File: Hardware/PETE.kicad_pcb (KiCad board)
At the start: 4 copper layers, 16 parts, among them U3 LM66200DRLR, U4 MAX77827AEFD+T, U5 SC4215

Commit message: PCB Done
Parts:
- added 3V3: 3V3LED, Resistor_SMD:R_0402_1005Metric, F.Cu at (66.4, 39.7)
- added 3V3: TestPoint, TestPoint:TestPoint_Pad_D1.0mm, F.Cu at (54.7, 25.9)
- added 3V3: TestPoint, TestPoint:TestPoint_Pad_D1.0mm, F.Cu at (64.2, 31.0)
- added BBIN: TestPoint, TestPoint:TestPoint_Pad_D1.0mm, F.Cu at (62.6, 29.1)
- added BBIN: TestPoint, TestPoint:TestPoint_Pad_D1.0mm, F.Cu at (49.8, 37.1)
- added BOOT: Conn_01x02_Male, Connector_PinHeader_2.54mm:PinHeader_1x02_P2.54mm_Vertical, F.Cu at (71.6, 20.6)
- added C1: 10uF, Capacitor_SMD:C_0402_1005Metric, F.Cu at (64.7, 36.4)
- added C10: 0.1uF, Capacitor_SMD:C_0402_1005Metric, F.Cu at (75.4, 33.4)
- added C11: 0.1uF, Capacitor_SMD:C_0402_1005Metric, F.Cu at (73.5, 43.2)
- added C12: 4.2pF, Capacitor_SMD:C_0402_1005Metric, F.Cu at (68.3, 33.9)
- added C13: C, Capacitor_SMD:C_0402_1005Metric, F.Cu at (74.6, 30.1)
- added C14: C, Capacitor_SMD:C_0402_1005Metric, F.Cu at (70.7, 30.1)
- added C15: 100nF, Capacitor_SMD:C_0402_1005Metric, F.Cu at (62.4, 41.9)
- added C16: 10uF, Capacitor_SMD:C_0402_1005Metric, F.Cu at (63.3, 41.9)
- added C17: 47nF, Capacitor_SMD:C_0402_1005Metric, F.Cu at (51.0, 43.7)
- added C18: 0.1n, Capacitor_SMD:C_0402_1005Metric, F.Cu at (91.9, 41.1)
- added C19: 0.1n, Capacitor_SMD:C_0402_1005Metric, F.Cu at (92.1, 50.0)
- added C2: 1uF, Capacitor_SMD:C_0402_1005Metric, F.Cu at (68.0, 35.8)
- added C28: 0.1n, Capacitor_SMD:C_0402_1005Metric, F.Cu at (83.2, 50.8)
- added C29: 0.1n, Capacitor_SMD:C_0402_1005Metric, F.Cu at (94.4, 35.7)
- added C3: 0.1uF, Capacitor_SMD:C_0402_1005Metric, F.Cu at (63.5, 22.9)
- added C30: 0.1n, Capacitor_SMD:C_0402_1005Metric, F.Cu at (95.2, 27.7)
- added C31: 0.1n, Capacitor_SMD:C_0402_1005Metric, F.Cu at (98.4, 41.9)
- added C32: 0.1n, Capacitor_SMD:C_0402_1005Metric, F.Cu at (98.6, 50.7)
- added C33: 0.1n, Capacitor_SMD:C_0402_1005Metric, F.Cu at (89.4, 50.9)
- added C34: 0.1n, Capacitor_SMD:C_0402_1005Metric, F.Cu at (95.3, 21.3)
- added C35: 0.1n, Capacitor_SMD:C_0402_1005Metric, F.Cu at (95.4, 29.3)
- added C36: 100nF, Capacitor_SMD:C_0402_1005Metric, F.Cu at (70.2, 45.7)
- added C37: 100nF, Capacitor_SMD:C_0402_1005Metric, F.Cu at (68.3, 44.0)
- added C4: 1uF, Capacitor_SMD:C_0402_1005Metric, F.Cu at (64.7, 34.5)
- added C5: 0.1uF, Capacitor_SMD:C_0402_1005Metric, F.Cu at (65.7, 36.4)
- added C6: 0.1uF, Capacitor_SMD:C_0402_1005Metric, F.Cu at (66.7, 36.4)
- added C7: 1uF, Capacitor_SMD:C_0402_1005Metric, F.Cu at (70.2, 33.0)
- added C8: 0.1uF, Capacitor_SMD:C_0402_1005Metric, F.Cu at (70.3, 22.9)
- added C9: 10nF, Capacitor_SMD:C_0402_1005Metric, F.Cu at (70.2, 34.0)
- added D1: SM712_SOT23, Package_TO_SOT_SMD:SOT-23, F.Cu at (49.2, 41.0)
- added D2: SP0503BAHT, Package_TO_SOT_SMD:SOT-143, F.Cu at (75.3, 45.3)
- added Data+: TestPoint, TestPoint:TestPoint_Pad_D1.0mm, F.Cu at (69.5, 53.1)
- added Data-: TestPoint, TestPoint:TestPoint_Pad_D1.0mm, F.Cu at (69.4, 50.1)
- added EN: Conn_01x02_Male, Connector_PinHeader_2.54mm:PinHeader_1x02_P2.54mm_Vertical, F.Cu at (65.4, 20.6)
- added H1: MountingHole_Pad, MountingHole:MountingHole_3.2mm_M3_DIN965_Pad, F.Cu at (103.0, 53.1)
- added H2: MountingHole_Pad, MountingHole:MountingHole_3.2mm_M3_DIN965_Pad, F.Cu at (48.0, 53.1)
- added H3: MountingHole_Pad, MountingHole:MountingHole_3.2mm_M3_DIN965_Pad, F.Cu at (48.0, 22.1)
- added H4: MountingHole_Pad, MountingHole:MountingHole_3.2mm_M3_DIN965_Pad, F.Cu at (103.0, 22.1)
- added J1: RBUS, Connector_Molex:Molex_Mini-Fit_Jr_5566-06A_2x03_P4.20mm_Vertical, F.Cu at (64.8, 53.2)
- added J2: USB_C_Receptacle_USB2.0, Connector_USB:USB_C_Receptacle_Palconn_UTC16-G, F.Cu at (76.2, 51.1)
- added J3: Micro_SD_Card_Det, Connector_Card:microSD_HC_Hirose_DM3AT-SF-PEJM5, B.Cu at (86.5, 27.8)
- added JP1: TermJP, Jumper:SolderJumper-2_P1.3mm_Open_RoundedPad1.0x1.5mm, F.Cu at (52.8, 41.5)
- added L1: 2.0nH, Inductor_SMD:L_0402_1005Metric, F.Cu at (66.2, 34.9)
- added L2: 20nH, Inductor_SMD:L_0402_1005Metric, F.Cu at (72.2, 32.9)
- added MISO: TestPoint, TestPoint:TestPoint_Pad_D1.0mm, F.Cu at (82.9, 46.8)
- added MOSI: TestPoint, TestPoint:TestPoint_Pad_D1.0mm, F.Cu at (82.9, 43.0)
- added MTCK: TestPoint, TestPoint:TestPoint_Pad_D1.0mm, F.Cu at (78.2, 32.8)
- added MTDI: TestPoint, TestPoint:TestPoint_Pad_D1.0mm, F.Cu at (78.2, 28.6)
- added MTDO: TestPoint, TestPoint:TestPoint_Pad_D1.0mm, F.Cu at (78.2, 30.4)
- added MTMS: TestPoint, TestPoint:TestPoint_Pad_D1.0mm, F.Cu at (78.1, 26.7)
- added PS1: MPRLS0025PA00001A, PressureSensor:XDCR_MPRLS0025PA00001A, F.Cu at (86.4, 50.8)
- added PS2: MPRLS0025PA00001A, PressureSensor:XDCR_MPRLS0025PA00001A, F.Cu at (95.3, 50.8)
- added PS3: MPRLS0025PA00001A, PressureSensor:XDCR_MPRLS0025PA00001A, F.Cu at (95.1, 41.9)
- added PS4: MPRLS0025PA00001A, PressureSensor:XDCR_MPRLS0025PA00001A, F.Cu at (95.4, 32.5)
- added PS5: MPRLS0025PA00001A, PressureSensor:XDCR_MPRLS0025PA00001A, F.Cu at (95.3, 24.5)
- added R1: 10K, Resistor_SMD:R_0402_1005Metric, F.Cu at (66.3, 22.9)
- added R10: 60, Resistor_SMD:R_0603_1608Metric, F.Cu at (53.0, 39.5)
- added R11: 5.1k, Resistor_SMD:R_0402_1005Metric, F.Cu at (73.1, 46.0)
- added R12: 5.1k, Resistor_SMD:R_0402_1005Metric, F.Cu at (77.6, 46.5)
- added R13: 470, Resistor_SMD:R_0402_1005Metric, F.Cu at (78.6, 46.5)
- added R18: 10k, Resistor_SMD:R_0402_1005Metric, B.Cu at (78.1, 24.6)
- added R2: 470, Resistor_SMD:R_0402_1005Metric, F.Cu at (63.9, 40.2)
- added R3: 10K, Resistor_SMD:R_0402_1005Metric, F.Cu at (67.2, 38.2)
- added R4: 470, Resistor_SMD:R_0402_1005Metric, F.Cu at (65.4, 39.7)
- added R5: 47.5, Resistor_SMD:R_0402_1005Metric, F.Cu at (68.3, 33.0)
- added R6: 499, Resistor_SMD:R_0402_1005Metric, F.Cu at (74.4, 33.4)
- added R8: 0, Resistor_SMD:R_0603_1608Metric, F.Cu at (56.0, 44.7)
- added R9: 60, Resistor_SMD:R_0603_1608Metric, F.Cu at (53.0, 43.4)
- added RXD: TestPoint, TestPoint:TestPoint_Pad_D1.0mm, F.Cu at (68.7, 30.6)
- added SCLK: TestPoint, TestPoint:TestPoint_Pad_D1.0mm, F.Cu at (82.8, 44.9)
- added SS1: TestPoint, TestPoint:TestPoint_Pad_D1.0mm, F.Cu at (82.9, 38.2)
- added SS2: TestPoint, TestPoint:TestPoint_Pad_D1.0mm, F.Cu at (85.1, 38.2)
- added SS3: TestPoint, TestPoint:TestPoint_Pad_D1.0mm, F.Cu at (87.3, 38.2)
- added SS4: TestPoint, TestPoint:TestPoint_Pad_D1.0mm, F.Cu at (80.8, 38.2)
- added SS5: TestPoint, TestPoint:TestPoint_Pad_D1.0mm, F.Cu at (78.6, 38.2)
- added TX: TX_LED, Resistor_SMD:R_0402_1005Metric, F.Cu at (63.5, 38.8)
- added TXD: TestPoint, TestPoint:TestPoint_Pad_D1.0mm, F.Cu at (68.7, 28.8)
- added U1: ESP32-S3, iclr:QFN40P700X700X90-57N, F.Cu at (73.5, 38.6)
- added U11: DPS310, iclr:XDCR_DPS310, F.Cu at (70.4, 44.0)
- added U2: SN65HVD230, Package_SO:SOIC-8_3.9x4.9mm_P1.27mm, F.Cu at (58.2, 41.2)
- added USB: USB_LED, Resistor_SMD:R_0402_1005Metric, F.Cu at (77.6, 44.6)
- added VBUS: TestPoint, TestPoint:TestPoint_Pad_D1.0mm, F.Cu at (60.1, 27.9)
- added Y1: 40MHz±10ppm, Crystal:Crystal_SMD_2016-4Pin_2.0x1.6mm, F.Cu at (72.6, 30.5)
- moved R17 146.5 mm to (49.1, 27.6), turned to 180 degrees
- moved R16 143.2 mm to (51.0, 27.6), turned to 180 degrees
- moved C27 140.8 mm to (52.8, 26.7), turned to 180 degrees
- moved C26 139.9 mm to (52.8, 27.6), turned to 180 degrees
- moved U5 139.7 mm to (50.9, 31.8), turned to 90 degrees
- moved C24 138.7 mm to (49.8, 35.9), turned to 180 degrees
- moved C25 134.8 mm to (51.9, 35.9), turned to 0 degrees
- moved C23 133.8 mm to (54.4, 31.2), turned to 90 degrees
- moved L3 131.6 mm to (57.0, 28.6), turned to 180 degrees
- moved U4 128.2 mm to (57.0, 32.3), turned to 90 degrees
- moved R15 126.0 mm to (57.2, 34.6), turned to 0 degrees
- moved C21 124.9 mm to (59.5, 31.0), turned to 90 degrees
- moved C22 122.9 mm to (59.2, 33.8), turned to -90 degrees
- moved R14 122.8 mm to (61.1, 30.2), turned to -90 degrees
- moved C20 121.3 mm to (60.2, 33.8), turned to -90 degrees
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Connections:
- net +3V3 renamed +3.3V
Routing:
- net /SCLK: track 0.00 -> 71.8 mm, vias 0 -> 7
- net /MOSI: track 0.00 -> 70.1 mm, vias 0 -> 7
- net /MISO: track 0.00 -> 69.8 mm, vias 0 -> 7
- net +3.3V: track 1.61 -> 46.6 mm, vias 1 -> 15
- net /SS5: track 0.00 -> 38.9 mm, vias 0 -> 3
- net /SS2: track 0.00 -> 37.3 mm, vias 0 -> 3
- net /SS4: track 0.00 -> 34.2 mm, vias 0 -> 3
- net /SS3: track 0.00 -> 33.8 mm, vias 0 -> 3
- net /SS1: track 0.00 -> 32.2 mm, vias 0 -> 3
- net /CHIP_PU: track 0.00 -> 28.7 mm, vias 0 -> 1
- net RBUS_uC_V: track 0.00 -> 28.0 mm, vias 0 -> 1
- net /BOOT: track 0.00 -> 25.9 mm, vias 0 -> 1
- net /TXD: track 0.00 -> 24.0 mm
- net /CAN-: track 0.00 -> 22.8 mm
- net GND: track 6.73 -> 27.7 mm, vias 8 -> 74
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- added copper zone on In2.Cu, net +3.3V
- added copper zone on B.Cu, net GND
- added copper zone on In1.Cu, net GND
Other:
- board outline added: 61 x 37 mm

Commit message: Review Changes Made (except for meme)
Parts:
- C18, C19, C28, C29, C30: value 0.1n -> 0.1u
- C31, C32, C33, C34, C35: value 0.1n -> 1n
- TP15: renamed from SCLK; moved to B.Cu
- TP16: renamed from MOSI; moved to B.Cu
- TP17: renamed from MISO; moved to B.Cu
- moved TXLED1 15.3 mm to (74.5, 28.0), turned to 180 degrees
- moved R2 14.9 mm to (72.6, 28.0), turned to 0 degrees
- moved TP9 7.81 mm to (76.2, 26.7)
- moved JP1 6.04 mm to (57.1, 37.2), turned to 0 degrees
- moved TP16 4.16 mm to (83.0, 47.2)
- moved TP15 2.64 mm to (81.4, 47.1), turned to 0 degrees
- moved TP17 2.31 mm to (81.7, 48.8), turned to 0 degrees
- moved C17 1.67 mm to (51.0, 42.0), turned to 90 degrees
- moved L1 1.45 mm to (67.6, 34.9)
- moved R9 1.45 mm to (53.0, 42.0)
- moved C4 1.08 mm to (65.7, 34.9), turned to 0 degrees
- moved R10 1.03 mm to (53.0, 40.5)
- moved D1 0.76 mm to (48.6, 41.5)
- moved C1 0.51 mm to (65.2, 36.3)
- moved C5 0.48 mm to (66.2, 36.3)
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- renumbered 3V3 to 3V3LED1, Data- to TP1, RXD to TP10, SS2 to TP11, SS1 to TP12, SS4 to TP13, SS5 to TP14, MTCK to TP18, MTDO to TP19, Data+ to TP2, MTDI to TP20, MTMS to TP21, SS3 to TP3, BBIN to TP4, 3V3 to TP5, 3V3 to TP6, VBUS to TP7, BBIN to TP8, TXD to TP9, TX to TXLED1, PS5 to U10, PS3 to U6, PS2 to U7, PS1 to U8, PS4 to U9, USB to USBLED1
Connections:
- U1 pad 36: unconnected-(U1-SPICLK_N/GPIO48-Pad36) -> /RES
- U10 pad 9: unconnected-(U10-RES-Pad9) -> /RES
- U6 pad 9: unconnected-(U6-RES-Pad9) -> /RES
- U7 pad 9: unconnected-(U7-RES-Pad9) -> /RES
- U8 pad 9: unconnected-(U8-RES-Pad9) -> /RES
- U9 pad 9: unconnected-(U9-RES-Pad9) -> /RES
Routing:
- net /RES: track 0.00 -> 71.7 mm
- net VBUS: track 15.2 -> 46.1 mm, vias 2 -> 5
- net /TXD: track 24.0 -> 8.22 mm
- net GND: track 27.7 -> 12.8 mm, vias 74 -> 71
- net Net-(JP1-B): track 5.25 -> 11.8 mm
- net /CAN+: track 19.5 -> 25.6 mm
- net /MOSI: track 70.1 -> 66.0 mm, vias 7 -> 6
- net /CAN-BUS/Vref: track 5.98 -> 2.41 mm
- net /MISO: track 69.8 -> 66.7 mm, vias 7 -> 6
- net /SCLK: track 71.8 -> 68.7 mm, vias 7 -> 6
- net +3.3V: track 46.6 -> 49.0 mm, vias 15 -> 17
- net /CHIP_PU: track 28.7 -> 27.2 mm
- net /SS3: track 33.8 -> 32.4 mm
- net /CAN-: track 22.8 -> 24.1 mm
- net Net-(C6-Pad1): track 5.67 -> 4.36 mm

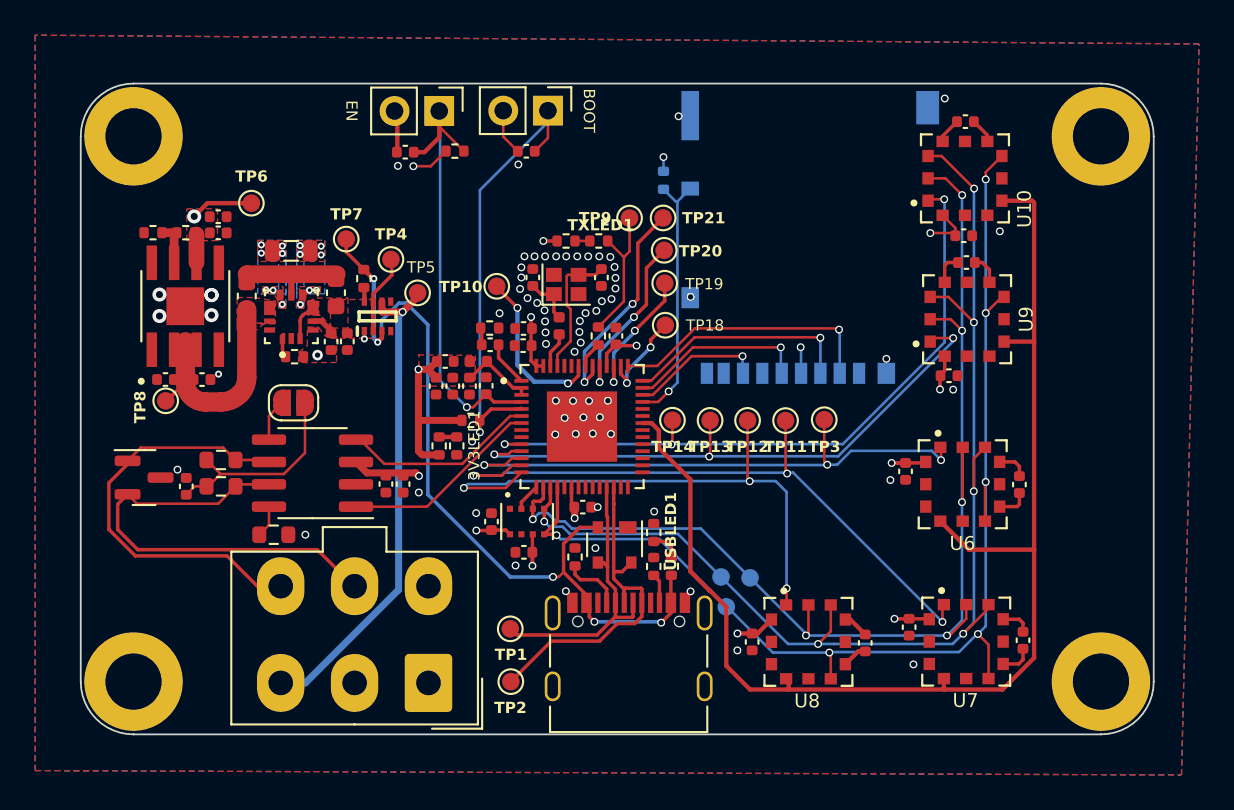
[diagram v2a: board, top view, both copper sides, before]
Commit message: Review Changes
Still don't know whats going on with the overlapping pours. Meme is a bit rubbish but it'll do for now.
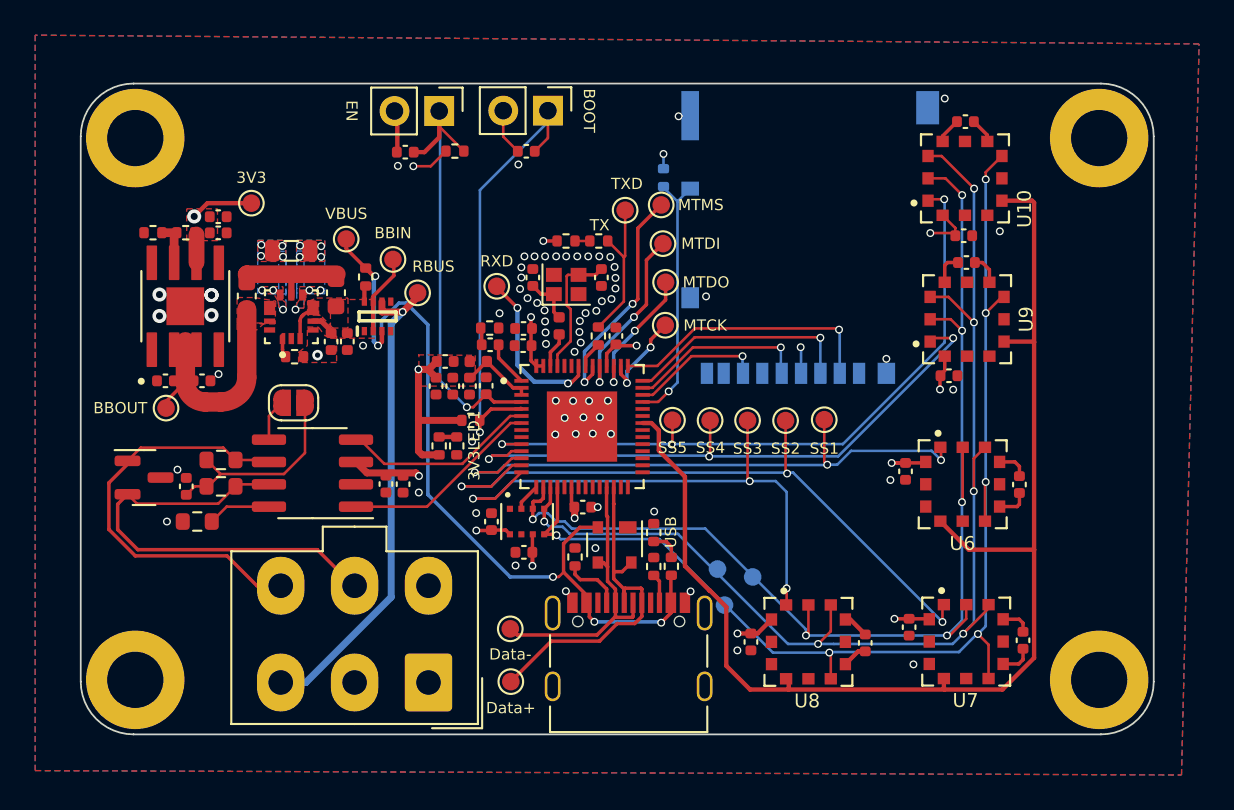
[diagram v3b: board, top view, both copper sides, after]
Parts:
- added G***: LOGO, iclr:PETE_LOGO, B.Cu at (63.5, 38.6)
- moved R8 4.41 mm to (51.6, 44.0), turned to 180 degrees
- moved TP21 0.75 mm to (78.0, 26.0), turned to 0 degrees
- moved TP9 0.51 mm to (76.0, 26.3)
- moved TP15 0.49 mm to (81.2, 46.7)
- moved TP8 0.41 mm to (49.9, 37.5)
- moved TP20 0.39 mm to (78.1, 28.2), turned to 0 degrees
- moved TP16 0.16 mm to (83.2, 47.1)
- moved R18 0.15 mm to (78.1, 24.4)
- moved TP17 0.14 mm to (81.6, 48.7)
- moved H2 0.14 mm to (48.1, 53.0)
- moved H3 0.14 mm to (48.1, 22.2)
- moved H1 0.14 mm to (102.9, 53.0)
- moved H4 0.14 mm to (102.9, 22.2)
- moved R14 0.14 mm to (61.2, 30.1)
- moved TP4 0.12 mm to (62.8, 29.1)
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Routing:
- net /SS2: track 37.3 -> 39.2 mm
- net Net-(U2-Rs): track 1.82 -> 3.60 mm
- net /SS1: track 32.2 -> 33.7 mm
- net VBUS: track 46.1 -> 46.9 mm
- net /SS4: track 34.2 -> 35.0 mm
- net /JTAG_MTMS: track 12.3 -> 13.0 mm
- net /SS3: track 32.4 -> 31.8 mm
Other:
- board text added: "Designed by Advay Prabhu!"
